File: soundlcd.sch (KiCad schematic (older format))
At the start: 36 parts, among them J10 Speaker, J8 GPIO3, J9 Audio out, SW3 BTN 1, SW4 BTN 2, U1 74HCT04, U13 AY-3-8910, U19 RTC72421, U20 ULN2803A, U21 74HC245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

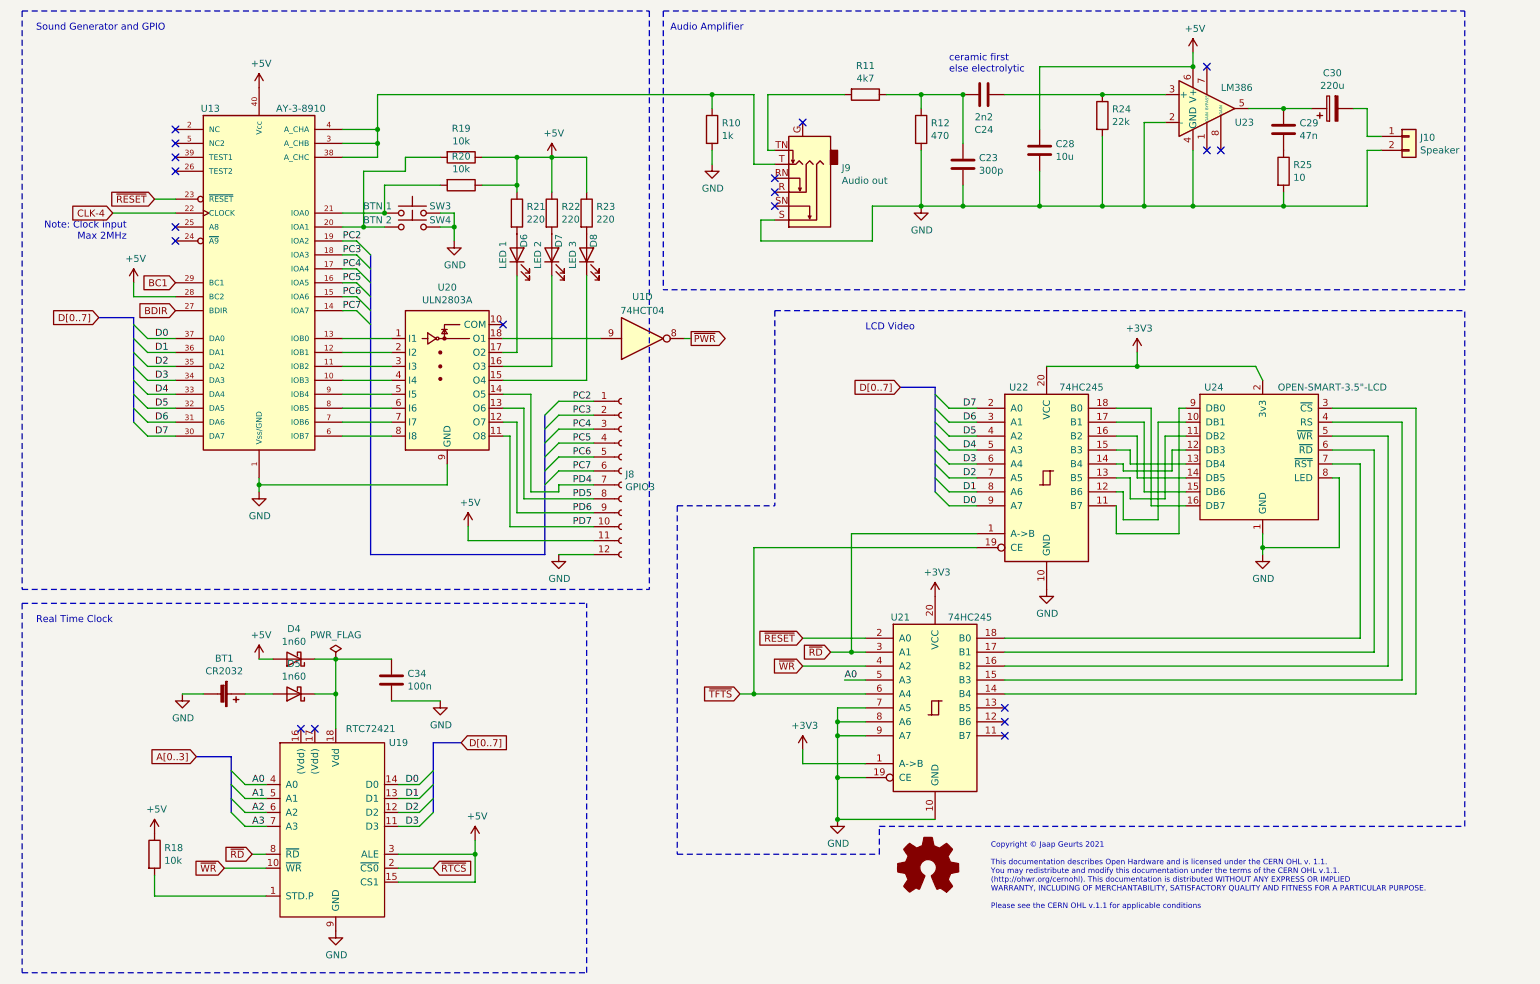
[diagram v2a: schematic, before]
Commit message: Bug fixes. Moved components two new sheet; added voltage monitor for RTC
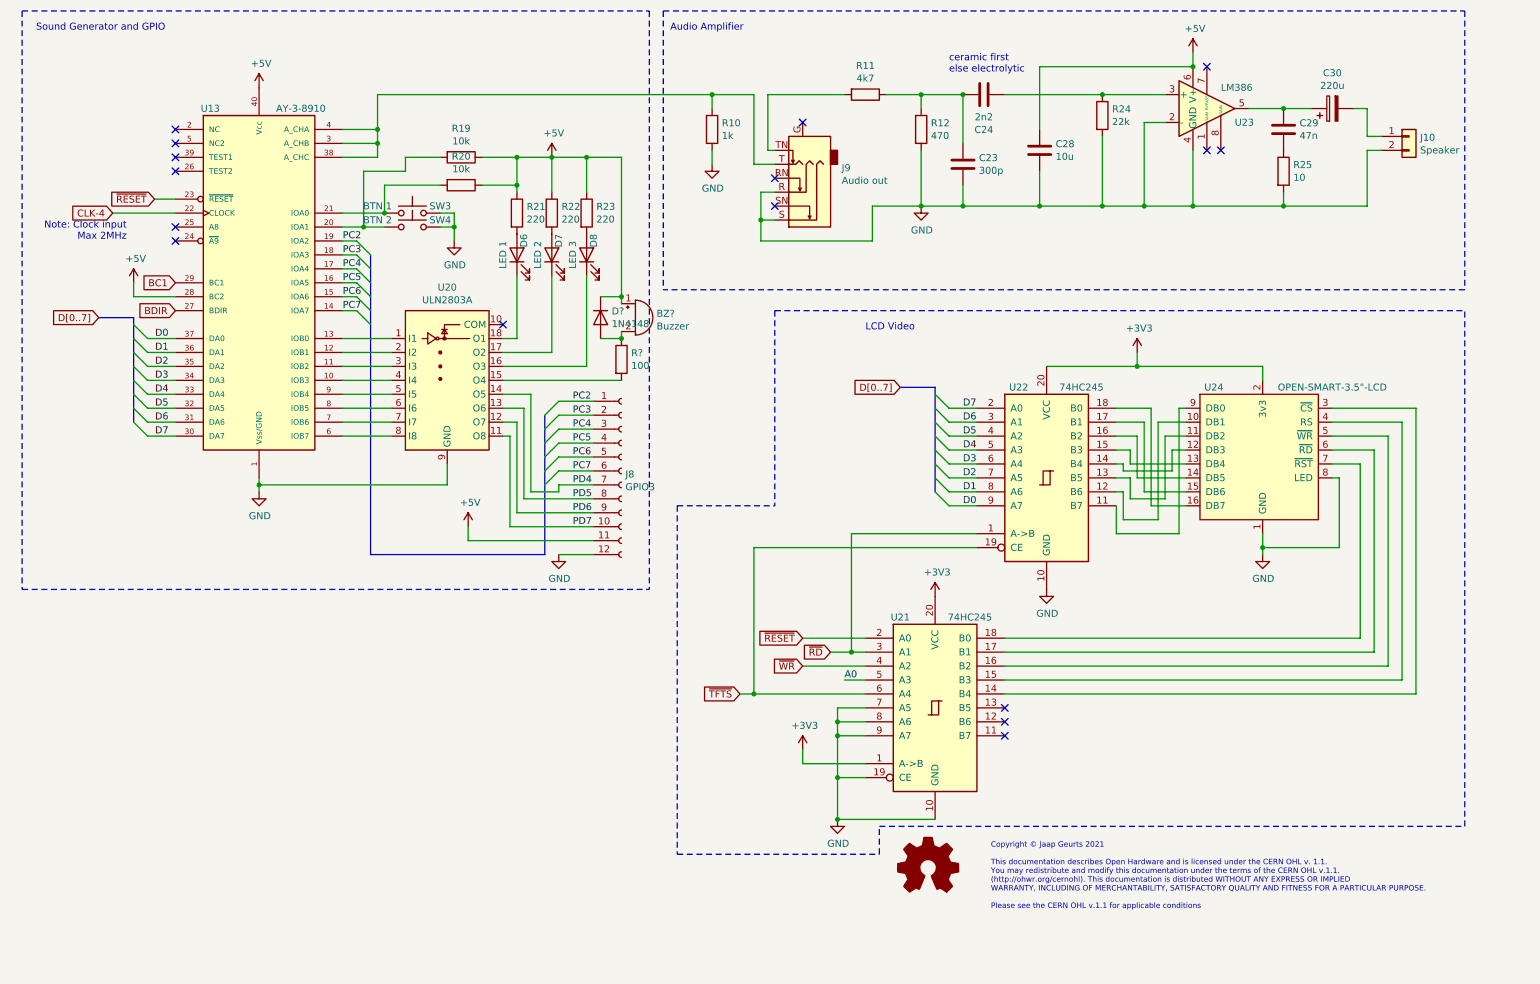
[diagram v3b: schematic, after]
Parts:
- removed BT1: CR2032, Battery:BatteryHolder_Keystone_106_1x20mm, symbol Device:Battery_Cell
- removed C34: 100n, Capacitor_THT:C_Disc_D5.0mm_W2.5mm_P2.50mm, symbol Device:C
- removed D4, D5: 1n60, Diode_THT:D_DO-35_SOD27_P7.62mm_Horizontal, symbol Diode:BAT42
- removed R18: 10k, Resistor_THT:R_Axial_DIN0207_L6.3mm_D2.5mm_P10.16mm_Horizontal, symbol Device:R
- removed U1: 74HCT04, Package_DIP:DIP-14_W7.62mm_Socket, symbol 74xx:74HCT04
- removed U19: RTC72421, Package_DIP:DIP-18_W7.62mm_Socket_LongPads, symbol personal:RTC72421
- added BZ?: Buzzer, symbol Device:Buzzer
- added D?: 1N4148, Diode_THT:D_DO-35_SOD27_P7.62mm_Horizontal, symbol Diode:1N4148
- added R?: 100, symbol Device:R
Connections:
- net +5V: now also BZ?.1 (-), D?.1 (K)
- net GND: now also J9.R
- net at U20.18 (O1): now also D6.1 (K)
- net at U20.15 (O4): now also R?.2; no longer D8.1 (K)
- net at U20.16 (O3): now also D8.1 (K); no longer D7.1 (K)
- net at U20.17 (O2): now also D7.1 (K); no longer D6.1 (K)
- new net: BZ?.2 (+), D?.2 (A), R?.1
- no-connect marks 19 -> 16
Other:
- note removed: "Real Time Clock"

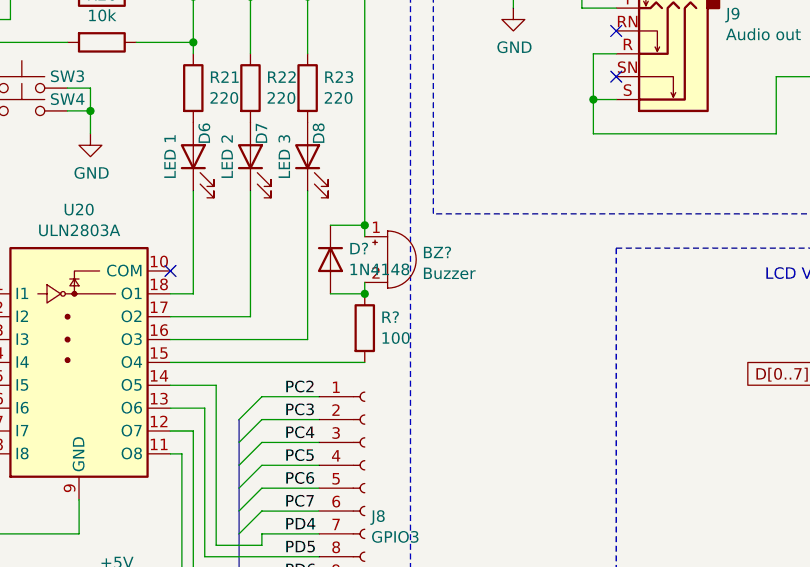
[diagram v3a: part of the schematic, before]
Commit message: Added RTC voltage detection circuit
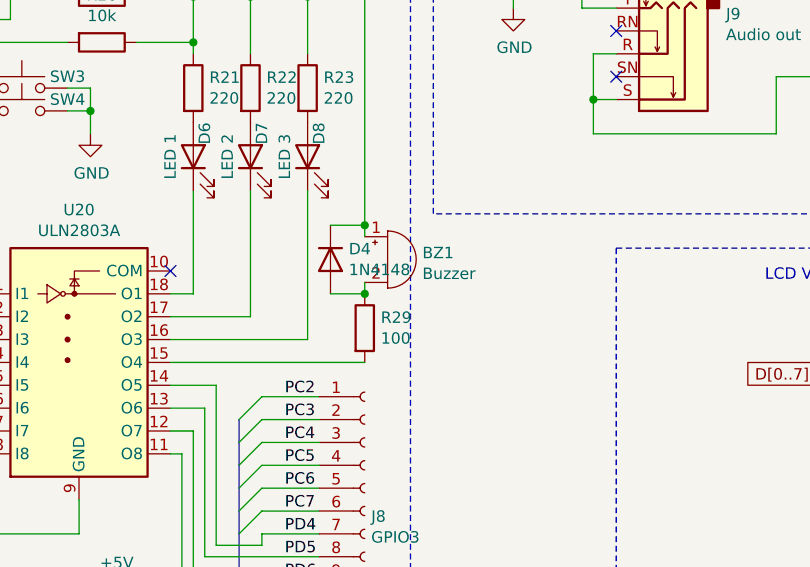
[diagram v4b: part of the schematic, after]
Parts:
- gave numbers to parts that had none: 3
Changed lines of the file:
@@
 encoding utf-8
 Sheet 4 6
-Title "Z80 Computer / Sound & I/O"
-Date "2021-02-02"
-Rev "2"
+Title "Z80 Computer"
+Date "2021-05-04"
+Rev "3"
 Comp "Jaap Geurts"
 Comment1 ""
@@
 	4200 3300 5050 3300
 $Comp
-L Device:Buzzer BZ?
+L Device:Buzzer BZ1
 U 1 1 60C7A00F
 P 5150 2850
-F 0 "BZ?" H 5302 2879 50  0000 L CNN
+F 0 "BZ1" H 5302 2879 50  0000 L CNN
 F 1 "Buzzer" H 5302 2788 50  0000 L CNN
 F 2 "" V 5125 2950 50  0001 C CNN
@@
 $EndComp
 $Comp
-L Device:R R?
+L Device:R R29
 U 1 1 60C7B1DD
 P 5050 3150
-F 0 "R?" H 5120 3196 50  0000 L CNN
+F 0 "R29" H 5120 3196 50  0000 L CNN
 F 1 "100" H 5120 3105 50  0000 L CNN
 F 2 "" V 4980 3150 50  0001 C CNN
@@
 	5050 2950 5050 3000
 $Comp
-L Diode:1N4148 D?
+L Diode:1N4148 D4
 U 1 1 60C9FC40
 P 4900 2850
-F 0 "D?" V 4854 2930 50  0000 L CNN
+F 0 "D4" V 4854 2930 50  0000 L CNN
 F 1 "1N4148" V 4945 2930 50  0000 L CNN
 F 2 "Diode_THT:D_DO-35_SOD27_P7.62mm_Horizontal" H 4900 2675 50  0001 C CNN
